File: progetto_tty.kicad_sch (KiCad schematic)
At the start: 7 parts, among them M1 Stepper_Motor_bipolar, M2 Stepper_Motor_bipolar, U1 ATmega328P-P, U2 L7805, Y1 16 MHz

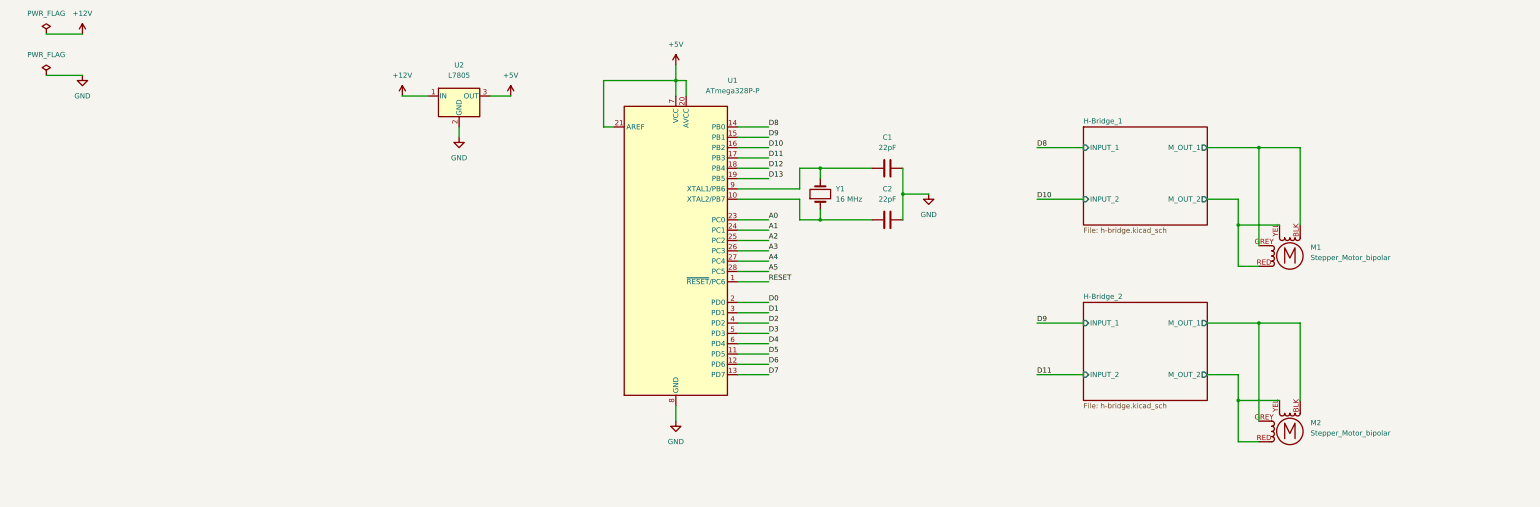
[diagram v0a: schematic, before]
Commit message: Small changes
Add decoupling caps, disconnect AREF from 5V, modify H-bridge resistor values
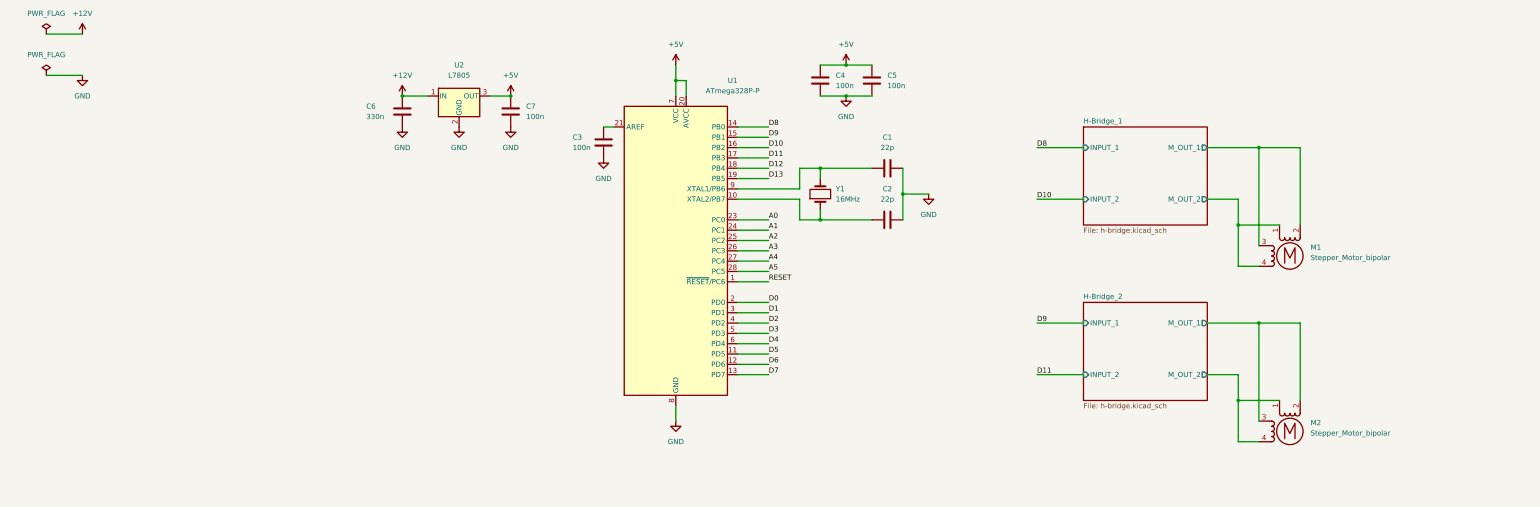
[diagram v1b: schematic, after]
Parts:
- added C3, C4, C5, C7: 100n, symbol Device:C
- added C6: 330n, symbol Device:C
- C1, C2: value 22pF -> 22p
- Y1: value 16 MHz -> 16MHz
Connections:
- net +12V: now also C6.1
- net +5V: now also C4.1, C5.1, C7.1; no longer U1.21 (AREF)
- net GND: now also C3.2, C4.2, C5.2, C6.2, C7.2
- net H-Bridge_1/M_OUT_1: now also M1.2 (-), M1.3; no longer M1.BLK (-), M1.GREY
- net H-Bridge_1/M_OUT_2: now also M1.1, M1.4; no longer M1.RED, M1.YEL
- net H-Bridge_2/M_OUT_1: now also M2.2 (-), M2.3; no longer M2.BLK (-), M2.GREY
- net H-Bridge_2/M_OUT_2: now also M2.1, M2.4; no longer M2.RED, M2.YEL
- new net: C3.1, U1.21 (AREF)
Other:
- moved on the sheet: M1, M2

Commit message: Replaced steppers with pin connector
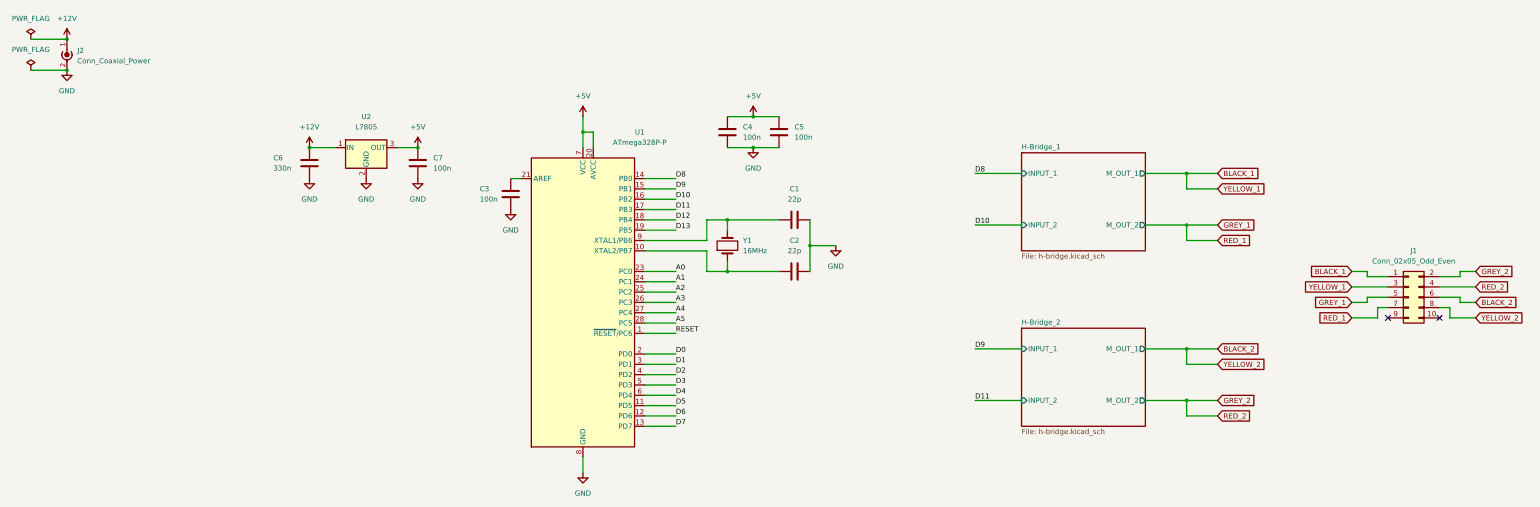
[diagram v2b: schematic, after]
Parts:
- removed M1, M2: Stepper_Motor_bipolar, symbol Motor:Stepper_Motor_bipolar
- added J1: Conn_02x05_Odd_Even, Connector_PinHeader_2.54mm:PinHeader_2x05_P2.54mm_Vertical, symbol Connector_Generic:Conn_02x05_Odd_Even
- added J2: Conn_Coaxial_Power, Connector_BarrelJack:BarrelJack_CUI_PJ-102AH_Horizontal, symbol Connector:Conn_Coaxial_Power
- C1, C2, C3, C4, C5, C7: footprint (none) -> Capacitor_THT:C_Disc_D5.0mm_W2.5mm_P5.00mm
- C6: footprint (none) -> Capacitor_THT:CP_Radial_D5.0mm_P2.00mm
- U2: footprint (none) -> Package_TO_SOT_THT:TO-220-3_Vertical
- Y1: footprint (none) -> Crystal:Crystal_HC49-U_Vertical
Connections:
- net +12V: now also J2.1 (In)
- net GND: now also J2.2 (Ext)
- new net BLACK_1: J1.1 (Pin_1), J1.3 (Pin_3)
- new net BLACK_2: J1.6 (Pin_6), J1.8 (Pin_8)
- new net GREY_1: J1.5 (Pin_5), J1.7 (Pin_7)
- new net GREY_2: J1.2 (Pin_2), J1.4 (Pin_4)
- no-connect marks 0 -> 2
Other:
- moved on the sheet: C1, C2, C3, C4, C5, C6, C7, U1, U2, Y1
